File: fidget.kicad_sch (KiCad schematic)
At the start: 10 parts, among them SW1 SW_Push, SW2 SW_Push, SW3 SW_Push, U1 XIAO-RP2040-DIP

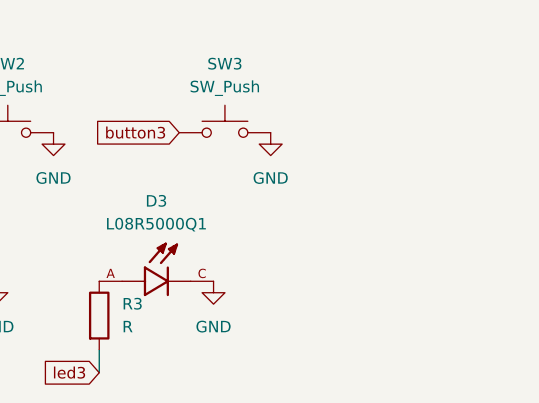
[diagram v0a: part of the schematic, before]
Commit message: add 3d models
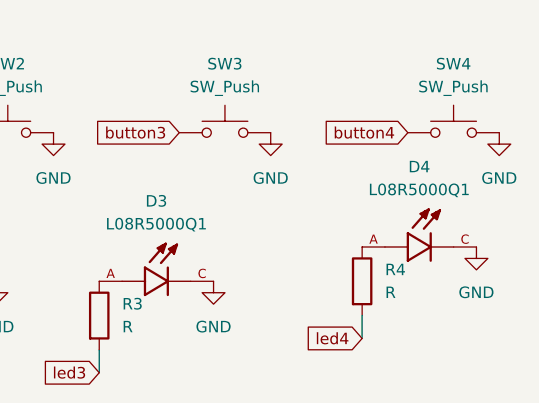
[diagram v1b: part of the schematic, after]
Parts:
- added D4: L08R5000Q1, general:LEDRD254W57D500H1070, symbol led:L08R5000Q1
- added R4: R, Resistor_THT:R_Axial_DIN0204_L3.6mm_D1.6mm_P5.08mm_Horizontal, symbol Device:R
- added SW4: SW_Push, general:SW_Cherry_MX_1.00u_PCB, symbol Switch:SW_Push
- SW1, SW2, SW3: footprint Button_Switch_Keyboard:SW_Cherry_MX_1.00u_PCB -> general:SW_Cherry_MX_1.00u_PCB
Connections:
- net GND: now also D4.C, SW4.2
- new net: D4.A, R4.1
- new net button4: SW4.1
- new net led4: R4.2

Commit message: actually add led models
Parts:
- D1, D2, D3, D4: footprint general:LEDRD254W57D500H1070 -> general:LEDRD254W57D500H1070_3d
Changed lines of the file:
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@@
 			)
 		)
-		(property "Footprint" "general:LEDRD254W57D500H1070"
+		(property "Footprint" "general:LEDRD254W57D500H1070_3d"
 			(at 170.18 110.49 0)
 			(effects
@@
 			)
 		)
-		(property "Footprint" "general:LEDRD254W57D500H1070"
+		(property "Footprint" "general:LEDRD254W57D500H1070_3d"
 			(at 214.63 110.49 0)
 			(effects
@@
 			)
 		)
-		(property "Footprint" "general:LEDRD254W57D500H1070"
+		(property "Footprint" "general:LEDRD254W57D500H1070_3d"
 			(at 190.5 110.49 0)
 			(effects
@@
 			)
 		)
-		(property "Footprint" "general:LEDRD254W57D500H1070"
+		(property "Footprint" "general:LEDRD254W57D500H1070_3d"
 			(at 243.84 106.68 0)
 			(effects

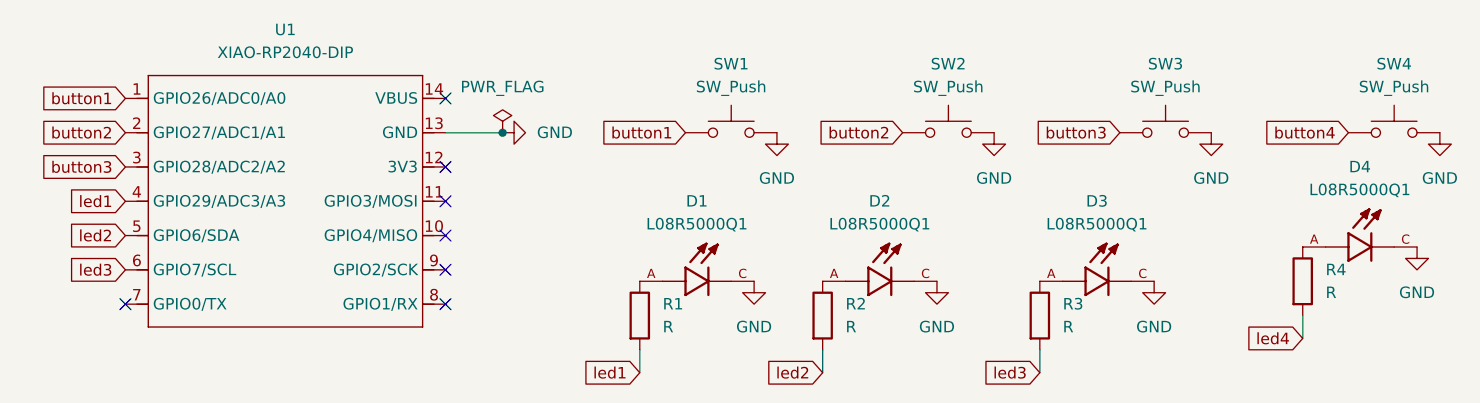
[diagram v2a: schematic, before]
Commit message: routing + ground plane
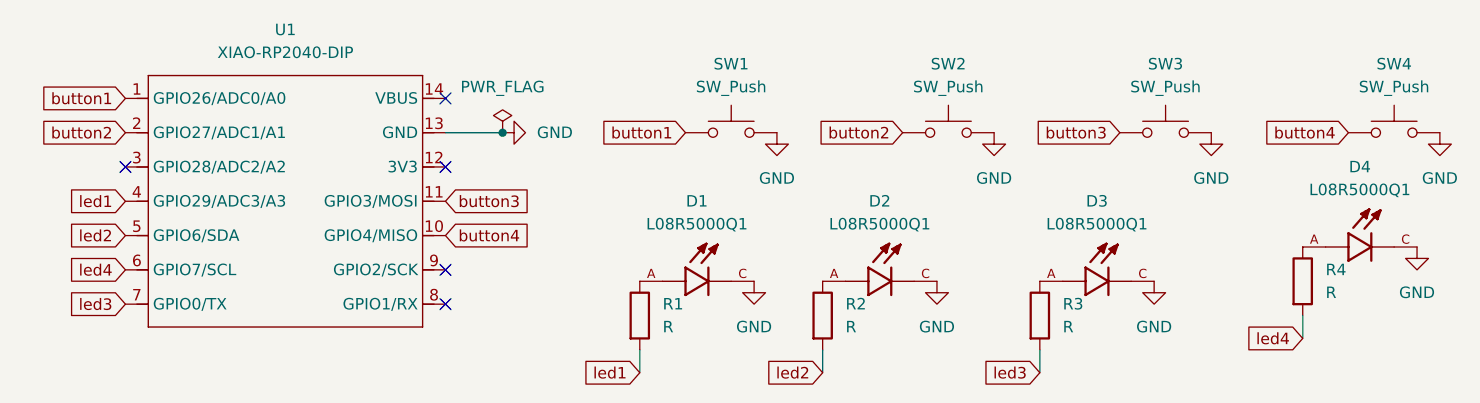
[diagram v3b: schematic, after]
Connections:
- net button3: now also U1.11 (GPIO3/MOSI); no longer U1.3 (GPIO28/ADC2/A2)
- net button4: now also U1.10 (GPIO4/MISO)
- net led3: now also U1.7 (GPIO0/TX); no longer U1.6 (GPIO7/SCL)
- net led4: now also U1.6 (GPIO7/SCL)
- no-connect marks 7 -> 5
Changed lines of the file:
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@@
 	)
 	(no_connect
-		(at 140.97 105.41)
+		(at 140.97 109.22)
+	)
+	(no_connect
+		(at 105.41 97.79)
+	)
+	(no_connect
+		(at 140.97 113.03)
 	)
 	(no_connect
@@
 	)
 	(no_connect
-		(at 140.97 113.03)
-	)
-	(no_connect
-		(at 140.97 109.22)
-	)
-	(no_connect
-		(at 140.97 101.6)
-	)
-	(no_connect
-		(at 105.41 113.03)
-	)
-	(no_connect
 		(at 140.97 97.79)
 	)
@@
 		)
 	)
+	(global_label "led3"
+		(shape input)
+		(at 105.41 113.03 180)
+		(fields_autoplaced yes)
+		(effects
+			(font
+				(size 1.27 1.27)
+			)
+			(justify right)
+		)
+		(property "Intersheetrefs" "${INTERSHEET_REFS}"
+			(at 98.3125 113.03 0)
+			(effects
+				(font
+					(size 1.27 1.27)
+				)
+				(justify right)
+				(hide yes)
+			)
+		)
+	)
 	(global_label "led1"
 		(shape input)
@@
 	(global_label "button3"
 		(shape input)
-		(at 105.41 97.79 180)
-		(fields_autoplaced yes)
-		(effects
-			(font
-				(size 1.27 1.27)
-			)
-			(justify right)
-		)
-		(property "Intersheetrefs" "${INTERSHEET_REFS}"
-			(at 95.1679 97.79 0)
-			(effects
-				(font
-					(size 1.27 1.27)
-				)
-				(justify right)
+		(at 140.97 101.6 0)
+		(fields_autoplaced yes)
+		(effects
+			(font
+				(size 1.27 1.27)
+			)
+			(justify left)
+		)
+		(property "Intersheetrefs" "${INTERSHEET_REFS}"
+			(at 151.2121 101.6 0)
+			(effects
+				(font
+					(size 1.27 1.27)
+				)
+				(justify left)
 				(hide yes)
 			)
@@
 		)
 	)
-	(global_label "led3"
+	(global_label "led4"
 		(shape input)
 		(at 105.41 109.22 180)
@@
 				(hide yes)
 			)
+		)
+	)
+	(global_label "button4"
+		(shape input)
+		(at 140.97 105.41 0)
+		(fields_autoplaced yes)
+		(effects
+			(font
+				(size 1.27 1.27)
+			)
+			(justify left)
+		)
+		(property "Intersheetrefs" "${INTERSHEET_REFS}"
+			(at 151.2121 105.41 0)
+			(effects
+				(font
+					(size 1.27 1.27)
+				)
+				(justify left)
+				(hide yes)
+			)
